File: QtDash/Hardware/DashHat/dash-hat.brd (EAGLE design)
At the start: 107.8 x 66.8 mm, 156 parts, among them IC1 LM324, IC2 MCP3X083008, IC3 MCP23017SS, IC4 LM358D, IC5 IL300, IC6 LM358D, IC7 IL300, IC8 LM358D, IC9 DS1374, J1 CONN_20X2, J10 455-1750-1-ND, J11 455-1750-1-ND, J15 455-1750-1-ND, J6 VOLVO_CONN_31, J7 VOLVO_CONN_32, J8 455-1750-1-ND, J9 455-1750-1-ND, Y1 ECX-.327-6-34RR

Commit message: - finished adding yageo resistors to schematic -- should all of the right part numbers now 	- TODO: caps
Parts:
- R1, R4, R57, R58, R6, R65, R69, R8: value 100 -> 100R; device SparkFun-Resistors:0603 -> digital_dash:0603
- R10, R11, R12, R2, R3, R5, R53, R54, R56, R59, R60, R62, R63, R64, R67, R68, R7, R71, R72, R73, R74, R75, R9: device SparkFun-Resistors:0603 -> digital_dash:0603
- R13, R14, R15, R16, R66, R70: value 640k -> 620k; device SparkFun-Resistors:0603 -> digital_dash:0603
- R17, R18, R19, R20, R21, R22, R23, R24, R25, R26, R27, R28, R29, R30, R31, R32, R33, R34, R35, R36, R37, R38, R39, R40, R41, R42, R43, R44, R45, R46, R47, R48, R49, R50, R51, R52: value 470 -> 470R; device SparkFun-Resistors:0603 -> digital_dash:0603
- R55, R61: value 10 -> 10R; device SparkFun-Resistors:0603 -> digital_dash:0603

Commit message: - added real part numbers for capacitors 	- made new BOM/parts list
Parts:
- C1, C17, C18, C2, C3, C4: value 10nF -> 10n; device SparkFun-Capacitors:0603 -> digital_dash:0603
- C10, C13, C14, C16, C20, C6, C8: value 1.0uF -> 1u; device SparkFun-Capacitors:0603 -> digital_dash:0603
- C11, C12, C15, C19, C5, C7, C9: value 0.1uF -> 100n; device SparkFun-Capacitors:0603 -> digital_dash:0603

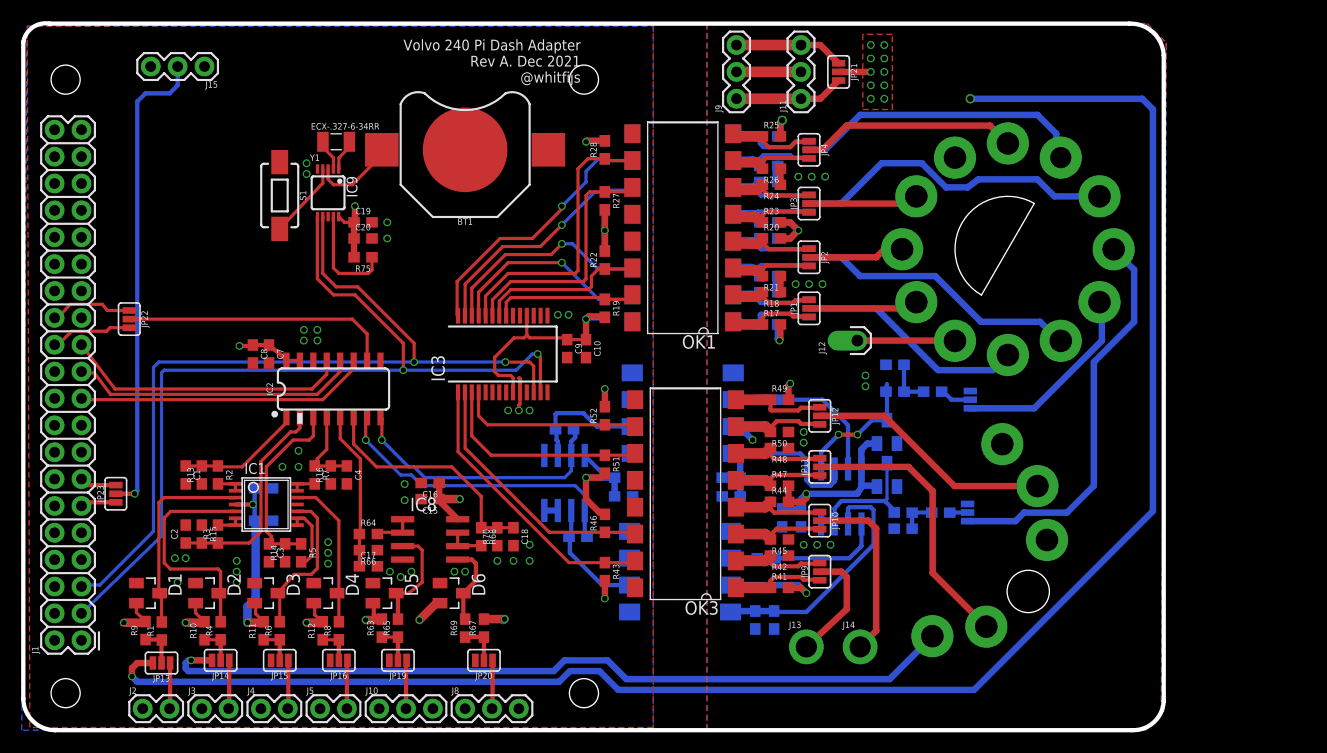
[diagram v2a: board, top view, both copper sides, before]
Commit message: - added load resistor to alternator D+ connection -- not sure what kind of current is needed for this -- 15 Ohm 5W EP5WS15RJ 17.5mm axial resistor spec'd for now
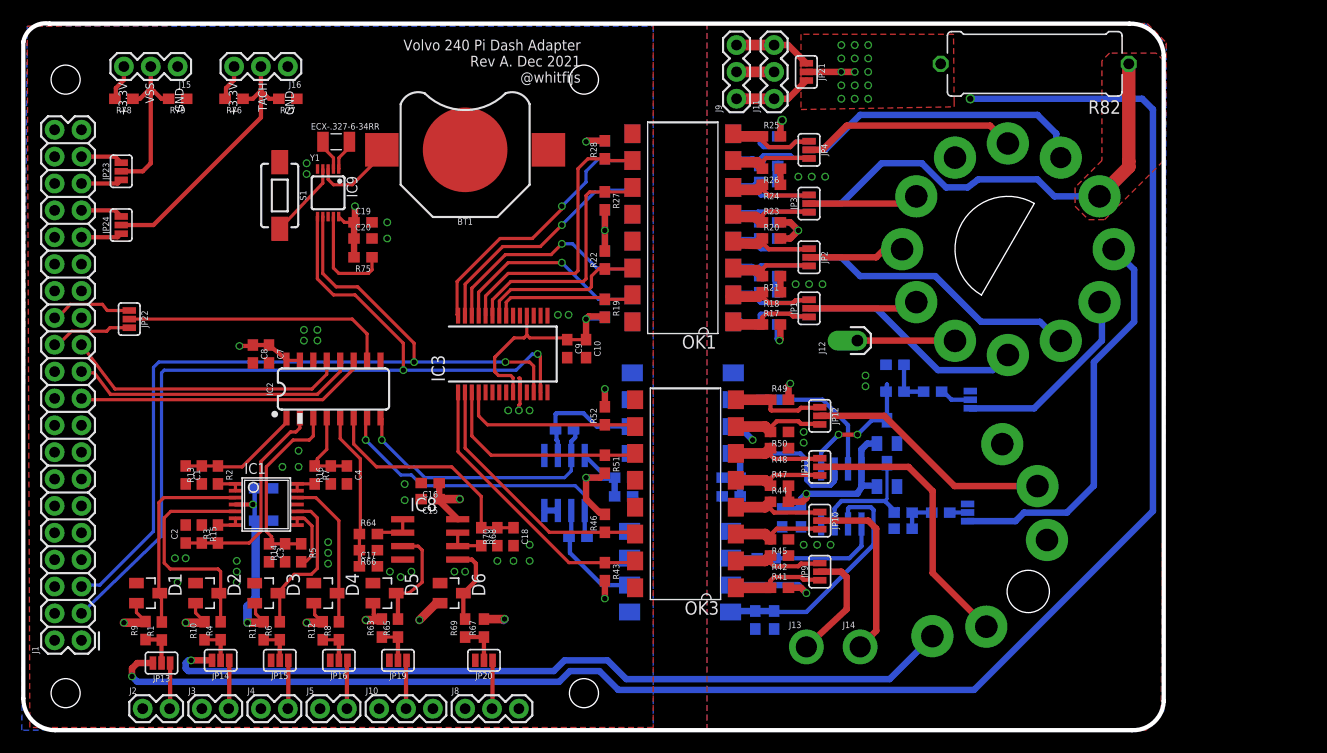
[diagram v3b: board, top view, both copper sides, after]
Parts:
- added J16: TACH_IN, SparkFun-Connectors:1X03
- added JP24: TACH_INPUT_SEL, SparkFun-Jumpers:SMT-JUMPER_3_NO_SILK
- added R76, R77, R78, R79: 1k, digital_dash:0603
- added R82: (no value), resistor:0617/17
- J15: value 455-1750-1-ND -> VSS_IN
- moved JP23 30.5 mm to (9.40, 52.8)
- moved JP21 3.05 mm to (74.2, 62.2)
- moved J15 2.54 mm to (14.7, 62.7)
- moved J11 2.54 mm to (71.1, 59.7)
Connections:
- new net GPIO13: J1.33, JP24.3
- new net GPIO19: J1.35, JP23.1
- new net GPIO26: J1.37, JP23.3
- new net GPIO6: J1.31, JP24.1
- new net N$43: J16.2, JP24.2, R76.1, R77.2
- net 12V: now also R82.2
- net 3.3V: now also J16.3, R76.2, R78.2
- net CHARGING_N: now also R82.1
- net GND: now also J16.1, R77.1, R79.1
- net GPIO17: no longer JP23.1
- net GPIO27: no longer JP23.3
- net N$33: now also R78.1, R79.2
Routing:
- net N$33: track 45.2 -> 16.3 mm, vias 1 -> 0
- net N$43: track 0.00 -> 26.3 mm
- net CHARGING_N: track 30.9 -> 44.6 mm
- net 3.3V: track 64.1 -> 70.9 mm
- net GPIO26: track 0.00 -> 3.99 mm
- net GPIO13: track 0.00 -> 3.99 mm
- net GPIO6: track 0.00 -> 3.90 mm
- net GPIO19: track 0.00 -> 3.90 mm
- net N$14: track 10.4 -> 7.32 mm
- net N$10: track 10.4 -> 7.32 mm
- net GPIO17: track 3.39 -> 0.48 mm
- net GPIO27: track 3.49 -> 0.81 mm
- net N$12: track 6.10 -> 3.56 mm
- net 12V: track 51.0 -> 52.5 mm, vias 17 -> 22
- added copper zone on layer 1, net CHARGING_N
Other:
- board text added: "+3.3V"
- board text added: "GND"
- board text added: "TACH"
- board text added: "VSS"

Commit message: - added sftp and networking to linux image -- should be able to ssh over ehternet now 	- made some final edits to the board and sent off to OSHPark 	- created a real rootfs overlay in boards/volvodash -- still need to work out how to load the cmdline and config files to the boot partition without hardcoding paths
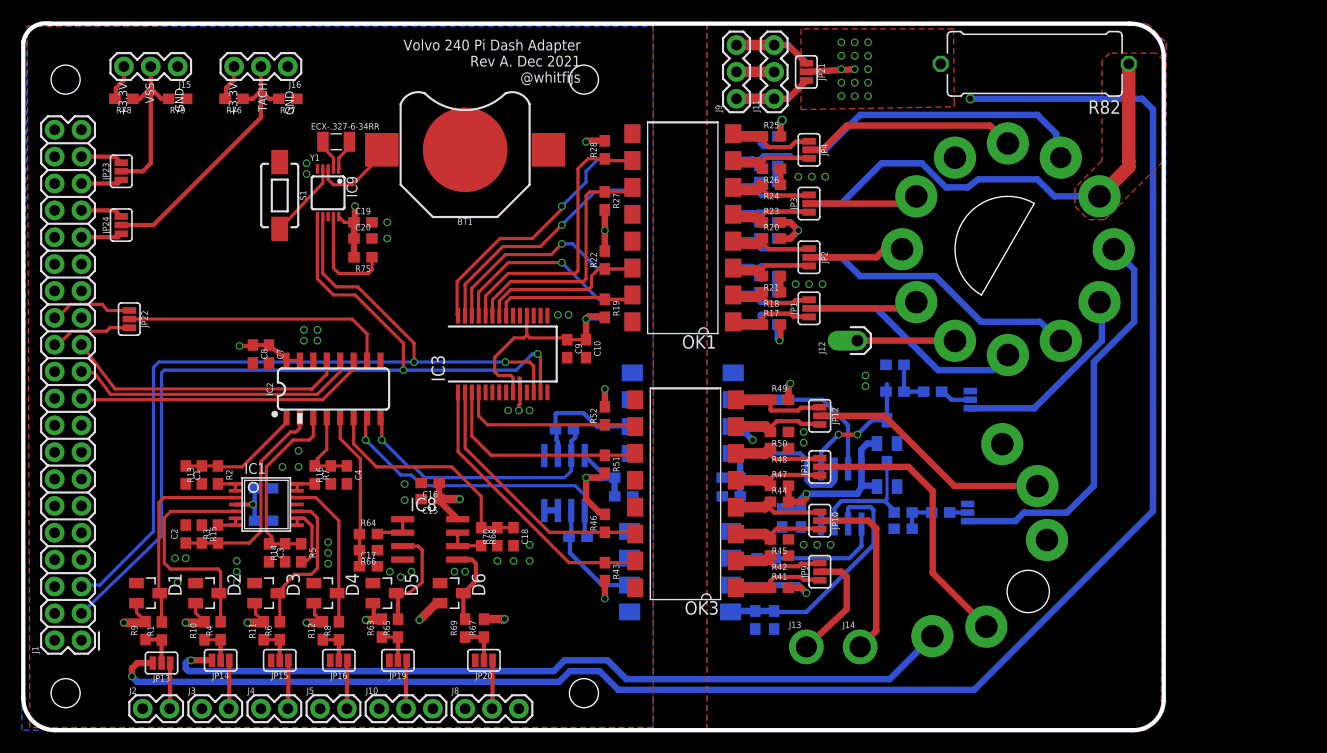
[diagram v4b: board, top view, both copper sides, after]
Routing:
- net 5V: track 44.7 -> 34.7 mm
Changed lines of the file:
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@@
 <layers>
 <layer number="1" name="Top" color="4" fill="1" visible="yes" active="yes"/>
-<layer number="2" name="Route2" color="1" fill="3" visible="yes" active="yes"/>
+<layer number="2" name="Route2" color="1" fill="3" visible="no" active="yes"/>
 <layer number="3" name="Route3" color="4" fill="3" visible="no" active="no"/>
 <layer number="4" name="Route4" color="1" fill="4" visible="no" active="no"/>
@@
 <layer number="13" name="Route13" color="4" fill="5" visible="no" active="no"/>
 <layer number="14" name="Route14" color="1" fill="6" visible="no" active="no"/>
-<layer number="15" name="Route15" color="4" fill="6" visible="yes" active="yes"/>
-<layer number="16" name="Bottom" color="9" fill="1" visible="no" active="yes"/>
+<layer number="15" name="Route15" color="4" fill="6" visible="no" active="yes"/>
+<layer number="16" name="Bottom" color="9" fill="1" visible="yes" active="yes"/>
 <layer number="17" name="Pads" color="2" fill="1" visible="yes" active="yes"/>
 <layer number="18" name="Vias" color="2" fill="1" visible="yes" active="yes"/>
@@
 <wire x1="22.86" y1="10.248" x2="22.772" y2="10.16" width="0.8128" layer="1"/>
 <wire x1="22.772" y1="10.16" x2="21.336" y2="10.16" width="0.8128" layer="1"/>
-<via x="21.336" y="10.16" extent="1-16" drill="0.5"/>
 <wire x1="28.448" y1="10.248" x2="28.36" y2="10.16" width="0.8128" layer="1"/>
 <wire x1="28.36" y1="10.16" x2="26.924" y2="10.16" width="0.8128" layer="1"/>
 <via x="26.924" y="10.16" extent="1-16" drill="0.5"/>
-<wire x1="22.01" y1="19.812" x2="22.098" y2="19.724" width="0.8128" layer="16"/>
-<wire x1="22.098" y1="19.724" x2="22.098" y2="12.446" width="0.8128" layer="16"/>
-<wire x1="22.098" y1="12.446" x2="21.336" y2="11.684" width="0.8128" layer="16"/>
-<wire x1="21.336" y1="11.684" x2="21.336" y2="10.16" width="0.8128" layer="16"/>
 <wire x1="34.036" y1="10.502" x2="33.948" y2="10.414" width="0.8128" layer="1"/>
 <wire x1="33.948" y1="10.414" x2="32.512" y2="10.414" width="0.8128" layer="1"/>
@@
 <vertex x="0" y="0"/>
 </polygon>
+<via x="21.336" y="10.16" extent="1-16" drill="0.5"/>
 </signal>
 <signal name="N$1">
@@
 <polygon width="0.3048" layer="15" isolate="0.3048">
 <vertex x="0.254" y="66.802"/>
-<vertex x="60.452" y="66.802"/>
-<vertex x="60.452" y="0"/>
+<vertex x="59.69" y="67.056"/>
+<vertex x="59.69" y="0.254"/>
 <vertex x="0.254" y="0"/>
 </polygon>
@@
 <contactref element="JP21" pad="2"/>
 <polygon width="0.3048" layer="1" isolate="0.3048" orphans="yes" thermals="no">
-<vertex x="73.66" y="65.786"/>
+<vertex x="73.66" y="66.294"/>
 <vertex x="73.66" y="58.674"/>
 <vertex x="88.138" y="58.928"/>
 <vertex x="88.138" y="59.376040625"/>
-<vertex x="88.078040625" y="65.786"/>
+<vertex x="88.078040625" y="66.294"/>
 </polygon>
-<via x="78.74" y="64.77" extent="1-16" drill="0.5"/>
-<via x="78.74" y="62.23" extent="1-16" drill="0.5"/>
-<via x="78.74" y="60.96" extent="1-16" drill="0.5"/>
-<via x="78.74" y="63.5" extent="1-16" drill="0.5"/>
-<via x="78.74" y="59.69" extent="1-16" drill="0.5"/>
+<via x="78.74" y="65.024" extent="1-16" drill="0.5"/>
+<via x="78.74" y="62.484" extent="1-16" drill="0.5"/>
+<via x="78.74" y="61.214" extent="1-16" drill="0.5"/>
+<via x="78.74" y="63.754" extent="1-16" drill="0.5"/>
+<via x="78.74" y="59.944" extent="1-16" drill="0.5"/>
 <wire x1="79.375" y1="23.114" x2="79.375" y2="22.987" width="0.6096" layer="16"/>
-<wire x1="74.168" y1="62.23" x2="78.74" y2="62.23" width="0.6096" layer="1"/>
-<via x="77.47" y="64.77" extent="1-16" drill="0.5"/>
-<via x="77.47" y="62.23" extent="1-16" drill="0.5"/>
-<via x="77.47" y="60.96" extent="1-16" drill="0.5"/>
-<via x="77.47" y="59.69" extent="1-16" drill="0.5"/>
+<wire x1="74.168" y1="62.23" x2="78.74" y2="62.484" width="0.6096" layer="1"/>
+<via x="77.47" y="65.024" extent="1-16" drill="0.5"/>
+<via x="77.47" y="62.484" extent="1-16" drill="0.5"/>
+<via x="77.47" y="61.214" extent="1-16" drill="0.5"/>
+<via x="77.47" y="59.944" extent="1-16" drill="0.5"/>
 <polygon width="0.3048" layer="2" isolate="0.3048">
 <vertex x="82.55" y="66.04"/>
@@
 <wire x1="80.754" y1="23.114" x2="79.375" y2="23.114" width="0.6096" layer="16"/>
 <contactref element="R82" pad="2"/>
-<via x="77.47" y="63.5" extent="1-16" drill="0.5"/>
-<via x="80.01" y="64.77" extent="1-16" drill="0.5"/>
-<via x="80.01" y="63.5" extent="1-16" drill="0.5"/>
-<via x="80.01" y="62.23" extent="1-16" drill="0.5"/>
-<via x="80.01" y="60.96" extent="1-16" drill="0.5"/>
-<via x="80.01" y="59.69" extent="1-16" drill="0.5"/>
+<via x="77.47" y="63.754" extent="1-16" drill="0.5"/>
+<via x="80.01" y="65.024" extent="1-16" drill="0.5"/>
+<via x="80.01" y="63.754" extent="1-16" drill="0.5"/>
+<via x="80.01" y="62.484" extent="1-16" drill="0.5"/>
+<via x="80.01" y="61.214" extent="1-16" drill="0.5"/>
+<via x="80.01" y="59.944" extent="1-16" drill="0.5"/>
 </signal>
 <signal name="OUT1">

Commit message: bugfix/hardware-revA-issues: 	- updated library to include TSV912 and LMV614 (RRIO -- what should have been in there to begin with) 	- made room for ethernet port 	- added ground planes where available in middle layers 	- moved traces away from mounting holes
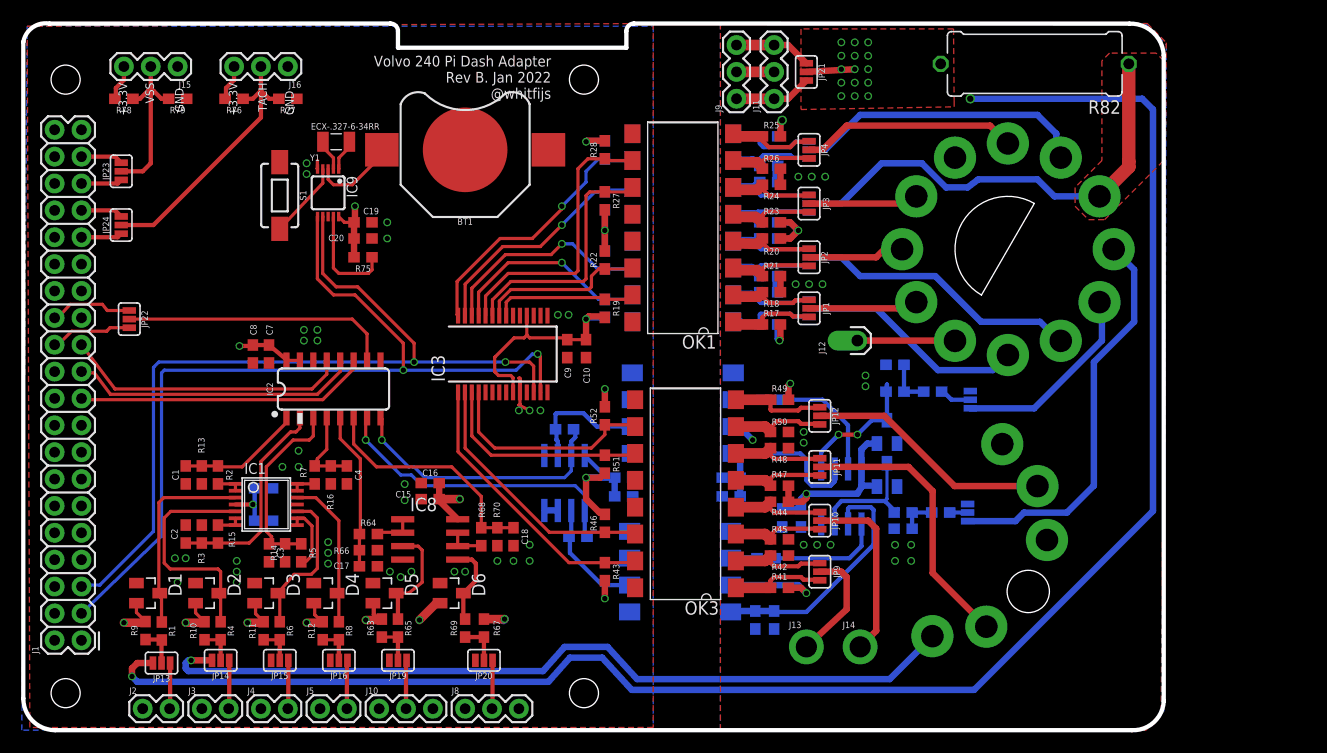
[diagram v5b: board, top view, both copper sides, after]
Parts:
- IC1: value LM324 -> LMV614
- IC6, IC8: value LM358D -> TSV912D
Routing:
- net OUT12: track 17.4 -> 20.7 mm
- net GND: track 5.84 -> 7.30 mm
- net FUEL_LVL_SENDER: track 76.6 -> 77.9 mm
- net COOLANT_TEMP_SENSOR: track 169.7 -> 170.9 mm
- net GND-ISO: vias 13 -> 17
- added copper zone on layer 15, net GND-ISO
- added copper zone on layer 2, net N$40
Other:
- outline, holes or cut-outs redrawn
- board text added: "Volvo 240 Pi Dash Adapter Rev B. Jan 2022 @whitfijs"
- board text removed: "Volvo 240 Pi Dash Adapter Rev A. Dec 2021 @whitfijs"
